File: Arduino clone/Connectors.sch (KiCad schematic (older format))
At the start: 4 parts

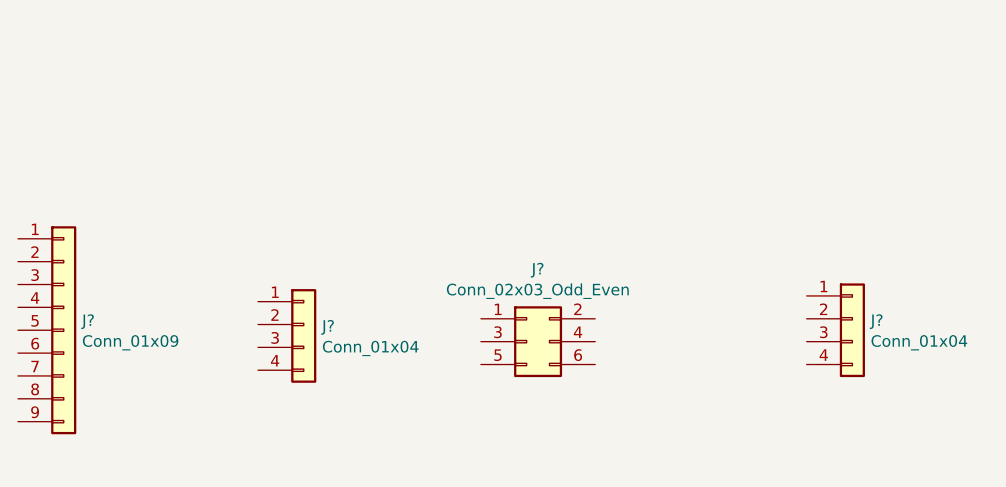
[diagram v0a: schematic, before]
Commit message: Arrange & Annotate
Arranged and annotated symbols in schematics.
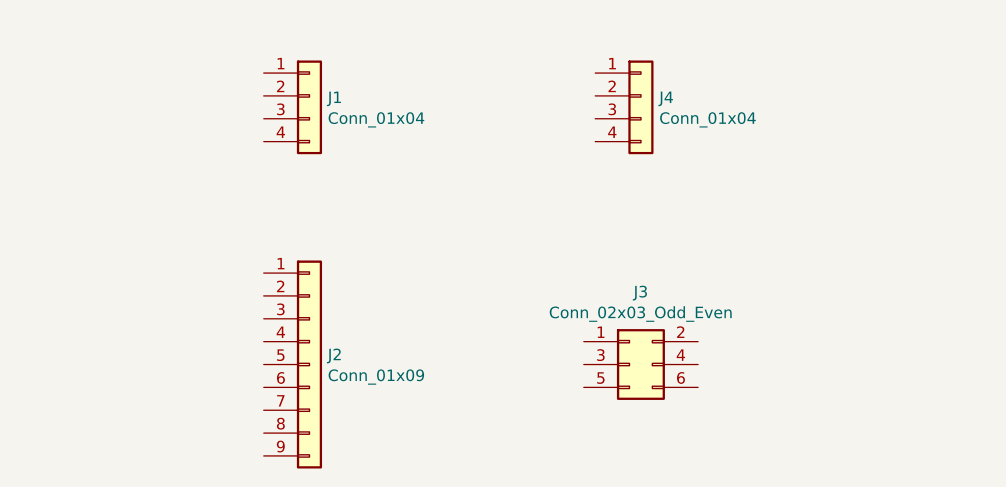
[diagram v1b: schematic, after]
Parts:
- gave numbers to parts that had none: 4
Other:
- moved on the sheet: J1, J2, J3, J4
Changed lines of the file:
@@
 $EndDescr
 $Comp
-L Connector_Generic:Conn_01x09 J?
+L Connector_Generic:Conn_01x09 J2
 U 1 1 5EDA2054
-P 4075 3850
-F 0 "J?" H 4155 3892 50  0000 L CNN
-F 1 "Conn_01x09" H 4155 3801 50  0000 L CNN
-F 2 "" H 4075 3850 50  0001 C CNN
-F 3 "~" H 4075 3850 50  0001 C CNN
-	1    4075 3850
+P 5150 4000
+F 0 "J2" H 5230 4042 50  0000 L CNN
+F 1 "Conn_01x09" H 5230 3951 50  0000 L CNN
+F 2 "" H 5150 4000 50  0001 C CNN
+F 3 "~" H 5150 4000 50  0001 C CNN
+	1    5150 4000
 	1    0    0    -1
 $EndComp
 $Comp
-L Connector_Generic:Conn_01x04 J?
+L Connector_Generic:Conn_01x04 J1
 U 1 1 5EDA282F
-P 5125 3825
-F 0 "J?" H 5205 3817 50  0000 L CNN
-F 1 "Conn_01x04" H 5205 3726 50  0000 L CNN
-F 2 "" H 5125 3825 50  0001 C CNN
-F 3 "~" H 5125 3825 50  0001 C CNN
-	1    5125 3825
+P 5150 2825
+F 0 "J1" H 5230 2817 50  0000 L CNN
+F 1 "Conn_01x04" H 5230 2726 50  0000 L CNN
+F 2 "" H 5150 2825 50  0001 C CNN
+F 3 "~" H 5150 2825 50  0001 C CNN
+	1    5150 2825
 	1    0    0    -1
 $EndComp
 $Comp
-L Connector_Generic:Conn_02x03_Odd_Even J?
+L Connector_Generic:Conn_02x03_Odd_Even J3
 U 1 1 5EDA3463
-P 6100 3900
-F 0 "J?" H 6150 4217 50  0000 C CNN
-F 1 "Conn_02x03_Odd_Even" H 6150 4126 50  0000 C CNN
-F 2 "" H 6100 3900 50  0001 C CNN
-F 3 "~" H 6100 3900 50  0001 C CNN
-	1    6100 3900
+P 6550 4000
+F 0 "J3" H 6600 4317 50  0000 C CNN
+F 1 "Conn_02x03_Odd_Even" H 6600 4226 50  0000 C CNN
+F 2 "" H 6550 4000 50  0001 C CNN
+F 3 "~" H 6550 4000 50  0001 C CNN
+	1    6550 4000
 	1    0    0    -1
 $EndComp
 $Comp
-L Connector_Generic:Conn_01x04 J?
+L Connector_Generic:Conn_01x04 J4
 U 1 1 5EDA382A
-P 7525 3800
-F 0 "J?" H 7605 3792 50  0000 L CNN
-F 1 "Conn_01x04" H 7605 3701 50  0000 L CNN
-F 2 "" H 7525 3800 50  0001 C CNN
-F 3 "~" H 7525 3800 50  0001 C CNN
-	1    7525 3800
+P 6600 2825
+F 0 "J4" H 6680 2817 50  0000 L CNN
+F 1 "Conn_01x04" H 6680 2726 50  0000 L CNN
+F 2 "" H 6600 2825 50  0001 C CNN
+F 3 "~" H 6600 2825 50  0001 C CNN
+	1    6600 2825
 	1    0    0    -1
 $EndComp

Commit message: Footprints & Values
Made footprint associations and added values to symbols.
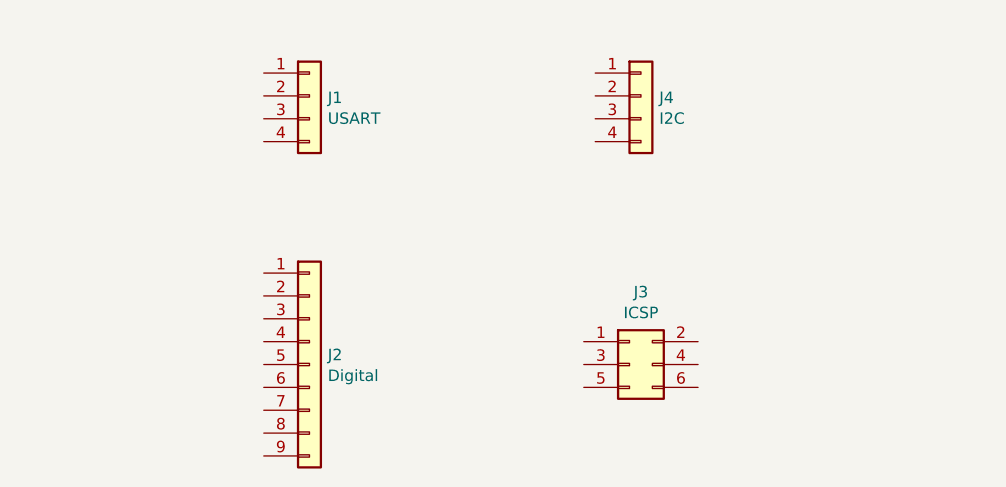
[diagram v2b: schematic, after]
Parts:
- J1: value Conn_01x04 -> USART; footprint (none) -> Connector_PinHeader_2.54mm:PinHeader_1x04_P2.54mm_Vertical
- J2: value Conn_01x09 -> Digital; footprint (none) -> Connector_PinHeader_2.54mm:PinHeader_1x09_P2.54mm_Vertical
- J3: value Conn_02x03_Odd_Even -> ICSP; footprint (none) -> Connector_PinHeader_2.54mm:PinHeader_2x03_P2.54mm_Vertical
- J4: value Conn_01x04 -> I2C; footprint (none) -> Connector_PinHeader_2.54mm:PinHeader_1x04_P2.54mm_Vertical
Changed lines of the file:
@@
 P 5150 4000
 F 0 "J2" H 5230 4042 50  0000 L CNN
-F 1 "Conn_01x09" H 5230 3951 50  0000 L CNN
-F 2 "" H 5150 4000 50  0001 C CNN
+F 1 "Digital" H 5230 3951 50  0000 L CNN
+F 2 "Connector_PinHeader_2.54mm:PinHeader_1x09_P2.54mm_Vertical" H 5150 4000 50  0001 C CNN
 F 3 "~" H 5150 4000 50  0001 C CNN
 	1    5150 4000
@@
 P 5150 2825
 F 0 "J1" H 5230 2817 50  0000 L CNN
-F 1 "Conn_01x04" H 5230 2726 50  0000 L CNN
-F 2 "" H 5150 2825 50  0001 C CNN
+F 1 "USART" H 5230 2726 50  0000 L CNN
+F 2 "Connector_PinHeader_2.54mm:PinHeader_1x04_P2.54mm_Vertical" H 5150 2825 50  0001 C CNN
 F 3 "~" H 5150 2825 50  0001 C CNN
 	1    5150 2825
@@
 P 6550 4000
 F 0 "J3" H 6600 4317 50  0000 C CNN
-F 1 "Conn_02x03_Odd_Even" H 6600 4226 50  0000 C CNN
-F 2 "" H 6550 4000 50  0001 C CNN
+F 1 "ICSP" H 6600 4226 50  0000 C CNN
+F 2 "Connector_PinHeader_2.54mm:PinHeader_2x03_P2.54mm_Vertical" H 6550 4000 50  0001 C CNN
 F 3 "~" H 6550 4000 50  0001 C CNN
 	1    6550 4000
@@
 P 6600 2825
 F 0 "J4" H 6680 2817 50  0000 L CNN
-F 1 "Conn_01x04" H 6680 2726 50  0000 L CNN
-F 2 "" H 6600 2825 50  0001 C CNN
+F 1 "I2C" H 6680 2726 50  0000 L CNN
+F 2 "Connector_PinHeader_2.54mm:PinHeader_1x04_P2.54mm_Vertical" H 6600 2825 50  0001 C CNN
 F 3 "~" H 6600 2825 50  0001 C CNN
 	1    6600 2825

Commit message: Wiring
Made the wiring of the schematic.
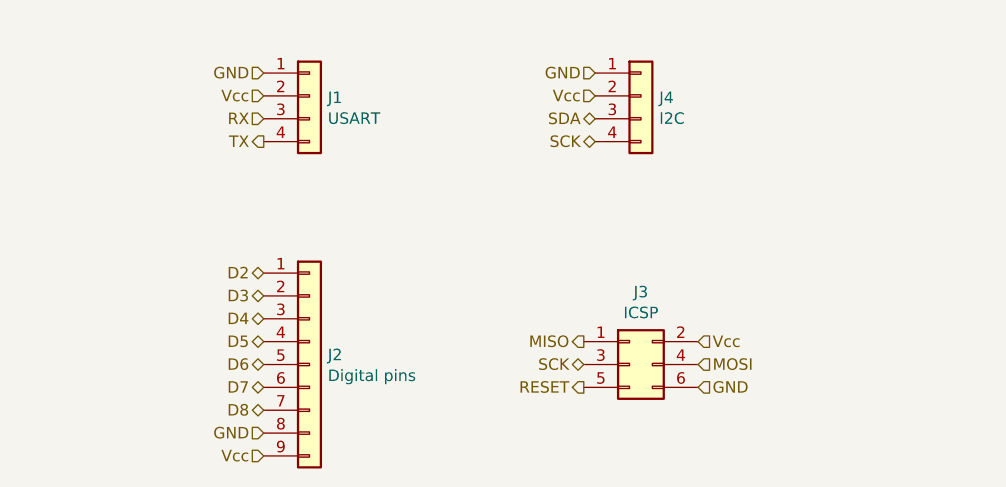
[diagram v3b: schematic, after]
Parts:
- J2: value Digital -> Digital pins
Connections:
- net D2: now reaches J2.1 (Pin_1)
- net D3: now reaches J2.2 (Pin_2)
- net D4: now reaches J2.3 (Pin_3)
- net D5: now reaches J2.4 (Pin_4)
- net D6: now reaches J2.5 (Pin_5)
- net D7: now reaches J2.6 (Pin_6)
- net D8: now reaches J2.7 (Pin_7)
- net GND: now reaches J2.8 (Pin_8)
- net GND: now also J1.1 (Pin_1), J3.6 (Pin_6), J4.1 (Pin_1)
- net Vcc: now reaches J2.9 (Pin_9)
- net Vcc: now also J1.2 (Pin_2), J3.2 (Pin_2), J4.2 (Pin_2)
- net RX: now reaches J1.3 (Pin_3)
- net TX: now reaches J1.4 (Pin_4)
- net MISO: now reaches J3.1 (Pin_1)
- net SCK: now reaches J3.3 (Pin_3)
- net SCK: now also J4.4 (Pin_4)
- net MOSI: now reaches J3.4 (Pin_4)
- net RESET: now reaches J3.5 (Pin_5)
- net SDA: now reaches J4.3 (Pin_3)
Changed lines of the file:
@@
 P 5150 4000
 F 0 "J2" H 5230 4042 50  0000 L CNN
-F 1 "Digital" H 5230 3951 50  0000 L CNN
+F 1 "Digital pins" H 5230 3951 50  0000 L CNN
 F 2 "Connector_PinHeader_2.54mm:PinHeader_1x09_P2.54mm_Vertical" H 5150 4000 50  0001 C CNN
 F 3 "~" H 5150 4000 50  0001 C CNN
@@
 	1    0    0    -1
 $EndComp
+Text HLabel 6350 3900 0    50   Output ~ 0
+MISO
+Text HLabel 6350 4000 0    50   BiDi ~ 0
+SCK
+Text HLabel 6350 4100 0    50   Output ~ 0
+RESET
+Text HLabel 6850 3900 2    50   Input ~ 0
+Vcc
+Text HLabel 6850 4000 2    50   Input ~ 0
+MOSI
+Text HLabel 6850 4100 2    50   Input ~ 0
+GND
+Text HLabel 4950 2725 0    50   Input ~ 0
+GND
+Text HLabel 4950 2825 0    50   Input ~ 0
+Vcc
+Text HLabel 4950 2925 0    50   Input ~ 0
+RX
+Text HLabel 4950 3025 0    50   Output ~ 0
+TX
+Text HLabel 6400 2725 0    50   Input ~ 0
+GND
+Text HLabel 6400 2825 0    50   Input ~ 0
+Vcc
+Text HLabel 6400 2925 0    50   BiDi ~ 0
+SDA
+Text HLabel 6400 3025 0    50   BiDi ~ 0
+SCK
+Text HLabel 4950 3600 0    50   BiDi ~ 0
+D2
+Text HLabel 4950 3700 0    50   BiDi ~ 0
+D3
+Text HLabel 4950 3800 0    50   BiDi ~ 0
+D4
+Text HLabel 4950 3900 0    50   BiDi ~ 0
+D5
+Text HLabel 4950 4000 0    50   BiDi ~ 0
+D6
+Text HLabel 4950 4100 0    50   BiDi ~ 0
+D7
+Text HLabel 4950 4200 0    50   BiDi ~ 0
+D8
+Text HLabel 4950 4300 0    50   Input ~ 0
+GND
+Text HLabel 4950 4400 0    50   Input ~ 0
+Vcc
 $EndSCHEMATC

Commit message: Comments
Added block comments.
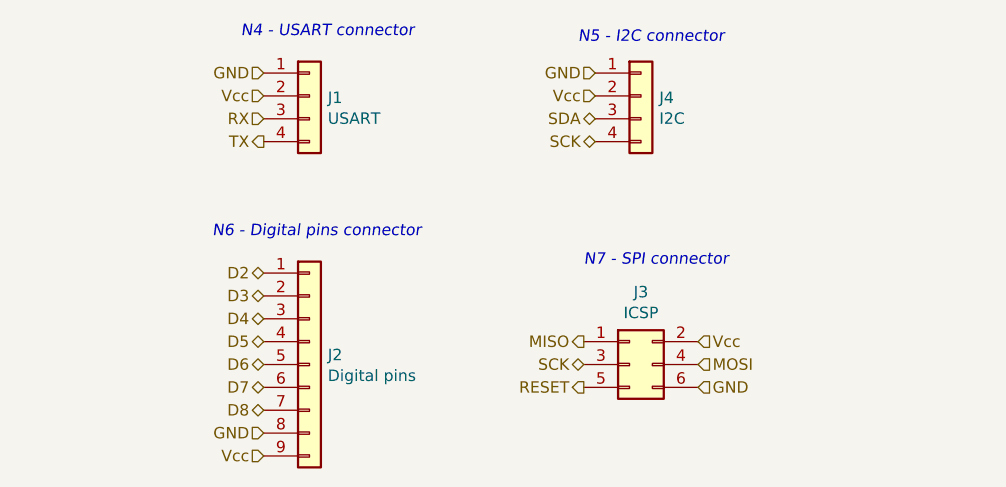
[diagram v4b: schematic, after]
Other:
- note added: "N4 - USART connector"
- note added: "N5 - I2C connector"
- note added: "N6 - Digital pins connector"
- note added: "N7 - SPI connector"
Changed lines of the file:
@@
 Text HLabel 4950 4400 0    50   Input ~ 0
 Vcc
+Text Notes 4850 2575 0    50   Italic 0
+N4 - USART connector
+Text Notes 6325 2600 0    50   Italic 0
+N5 - I2C connector
+Text Notes 4725 3450 0    50   Italic 0
+N6 - Digital pins connector
+Text Notes 6350 3575 0    50   Italic 0
+N7 - SPI connector
 $EndSCHEMATC
